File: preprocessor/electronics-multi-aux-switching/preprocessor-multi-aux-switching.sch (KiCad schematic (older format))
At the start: 21 parts, among them J1 Conn_01x03, J2 Conn_01x03, J3 Pinheader straight 1x08, J4 Conn_01x03, J5 Conn_01x03, J6 Conn_01x03, J7 Conn_01x03, J8 Conn_01x03, J9 Conn_01x03, T1 PMV30UN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

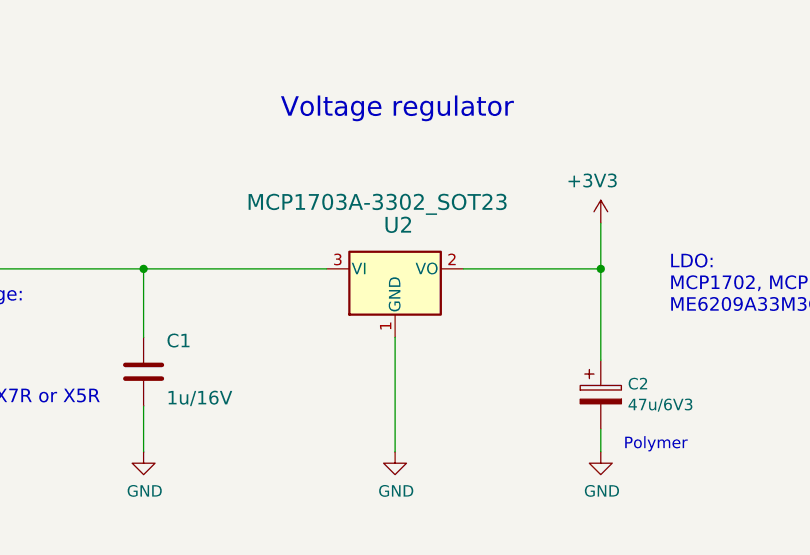
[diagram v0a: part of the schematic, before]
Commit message: Rename mk4s-mini5 to 5ch-PP-S
Otherwise people constantly confuse it with the mk4s-mini
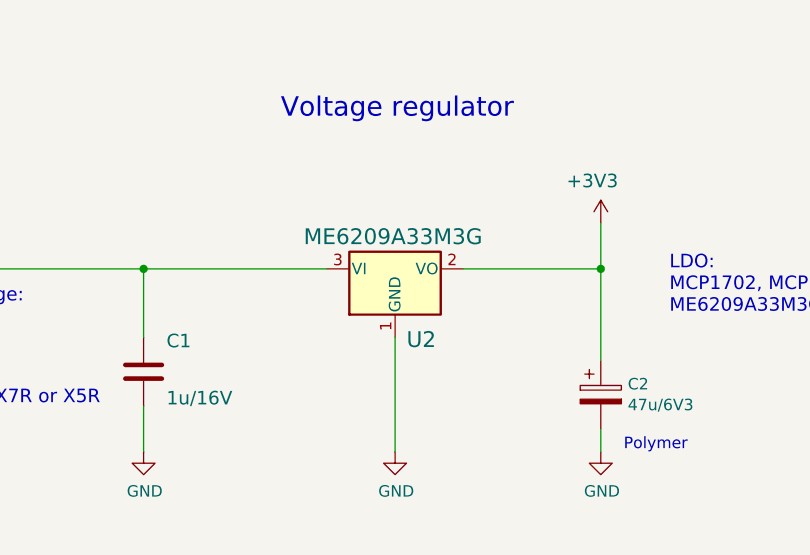
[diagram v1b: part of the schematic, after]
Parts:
- U2: value MCP1703A-3302_SOT23 -> ME6209A33M3G
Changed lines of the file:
@@
 U 1 1 09B5DC2D
 P 3750 2100
-F 0 "U2" H 3700 2250 69  0000 L BNN
-F 1 "MCP1703A-3302_SOT23" H 3100 2350 69  0000 L BNN
+F 0 "U2" H 3800 1750 69  0000 L BNN
+F 1 "ME6209A33M3G" H 3350 2200 69  0000 L BNN
 F 2 "Package_TO_SOT_SMD:SOT-23W" H 3750 2100 50  0001 C CNN
 F 3 "http://ww1.microchip.com/downloads/en/DeviceDoc/20005122B.pdf" H 3750 2100 50  0001 C CNN
